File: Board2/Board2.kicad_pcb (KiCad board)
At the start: 2 copper layers, 150 x 95 mm, 18 parts, among them J1 LEDs, J2 IR Therm, U1 MLX90614ESF-BCC-000-TU

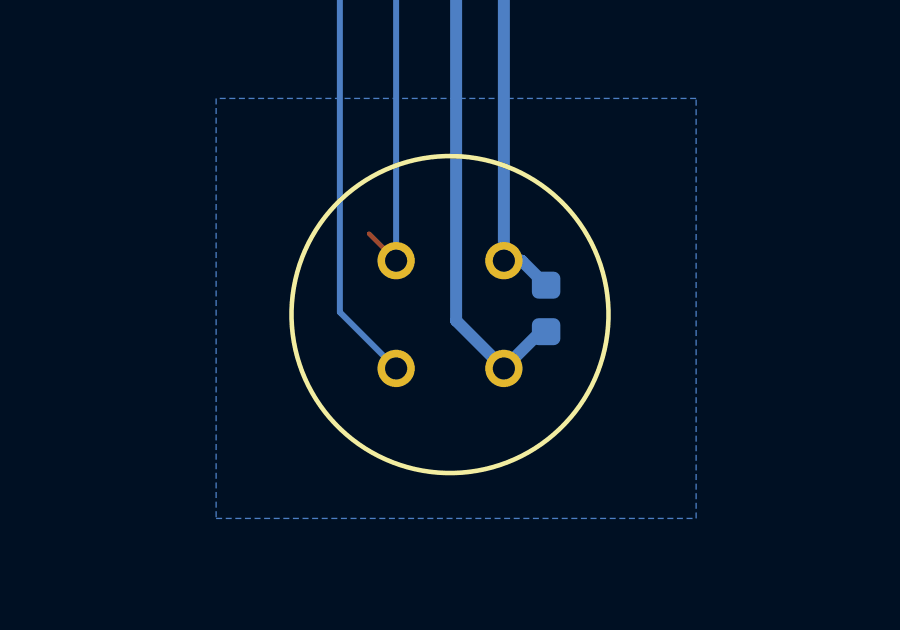
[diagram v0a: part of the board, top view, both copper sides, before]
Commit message: Resolve library and ERC issues
No changes to design.
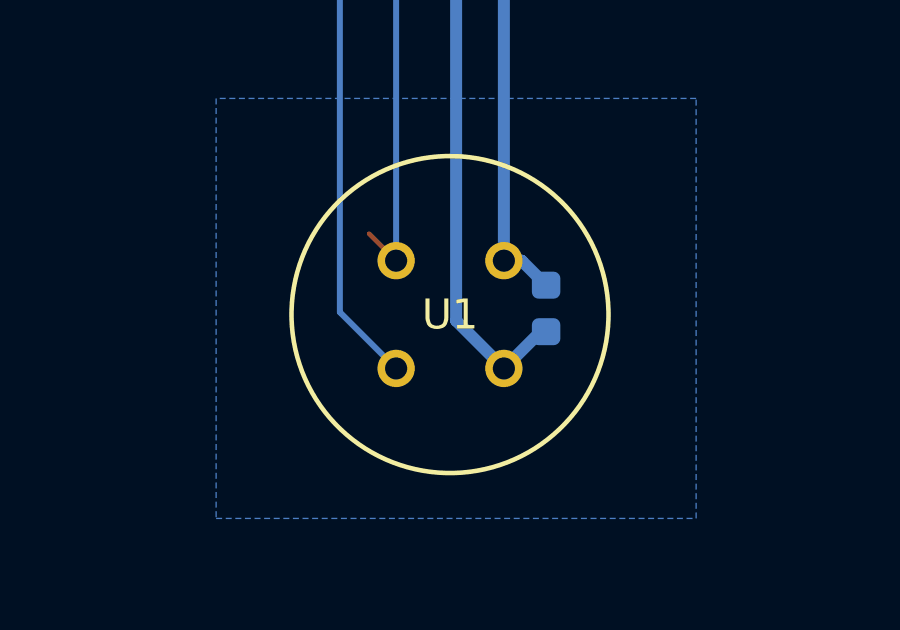
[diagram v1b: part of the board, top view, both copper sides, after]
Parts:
- U1: footprint Colins Library:MLX90614xCC_MEL -> 0_Project:IRTHERMO_MLX90614xCC_MEL
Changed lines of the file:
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@@
+			)
+		)
+		(property "Digikey_PN" ""
+			(at 0 0 180)
+			(unlocked yes)
+			(layer "F.Fab")
+			(hide yes)
+			(effects
+				(font
+					(size 1 1)
+					(thickness 0.15)
+				)
 			)
 		)
@@
 		)
 	)
-	(footprint "Colins Library:MLX90614xCC_MEL"
+	(footprint "0_Project:IRTHERMO_MLX90614xCC_MEL"
 		(layer "F.Cu")
 		(at 140 65.407897)
@@
 			(unlocked yes)
 			(layer "F.SilkS")
-			(hide yes)
 			(effects
 				(font
@@
 			)
 		)
-		(property "Footprint" "Colins Library:MLX90614xCC_MEL"
+		(property "Footprint" "0_Project:IRTHERMO_MLX90614xCC_MEL"
 			(at 0 0 0)
 			(layer "F.Fab")
@@
 		(fp_arc
 			(start 6.340061 -2.747958)
-			(mid 8.222251 1.796052)
+			(mid 8.222251 1.796051)
 			(end 6.340061 6.340061)
 			(stroke
@@
 		(model "${KIPRJMOD}/Library/3DModels/IRLED_MLX90614ESF-BCC-000-TU.step"
 			(offset
-				(xyz 1.7 -1.8 0)
+				(xyz 1.9 -1.8 0)
 			)
 			(scale

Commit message: v1.2 release of board with bug fixes etc
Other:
- board text added: "60x10mm (5V) Cooling fan hole and mounts (optional) DigiKey P/n: OD6010-05LB-ND"
- board text added: "IR Thermomemter {dblquote}Iris{dblquote} to underside of PTC plate"
- board text added: "Metal tab"
- board text added: "^"
